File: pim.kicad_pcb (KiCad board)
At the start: 2 copper layers, 96.4 x 66.5 mm, 13 parts, among them J1 DE9_Plug, J2 DE9_Plug, J3 Conn_01x20_Pin, J4 Conn_01x03_MountingPin, U1 RaspberryPi_Pico_W

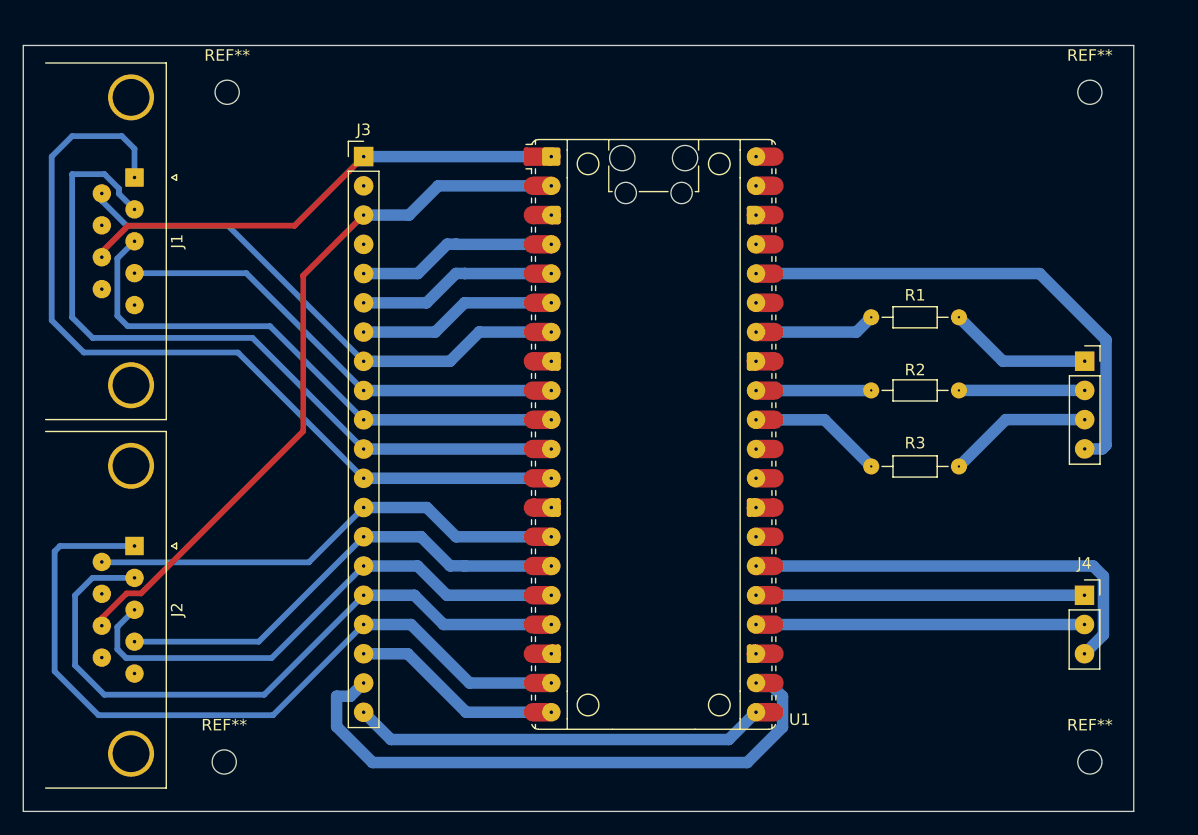
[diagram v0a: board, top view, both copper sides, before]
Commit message: improve some tracks cleareance
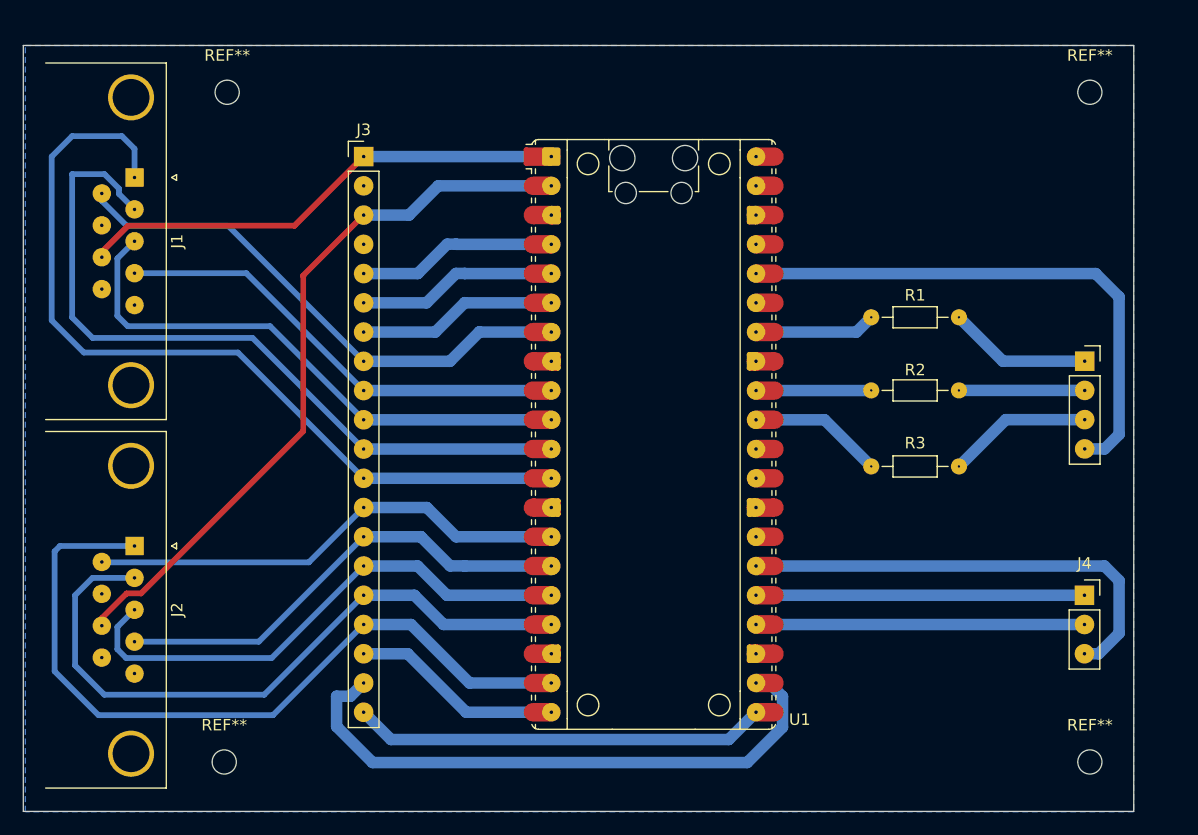
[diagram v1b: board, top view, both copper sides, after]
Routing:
- net Net-(D1-A): track 43.9 -> 47.8 mm
- net /PI-11: track 38.0 -> 40.4 mm
- added copper zone on B.Cu, net GNDPWR
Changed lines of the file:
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@@
 		(fp_arc
 			(start 10.579676 25.189937)
-			(mid 10.357946 25.493957)
+			(mid 10.35796 25.493961)
 			(end 10 25.61)
 			(stroke
@@
 	)
 	(segment
-		(start 108.166428 33.782)
-		(end 113.923428 39.539)
+		(start 115.062 35.814)
+		(end 115.062 47.752)
 		(width 1)
 		(layer "B.Cu")
@@
 	)
 	(segment
-		(start 113.597428 49.009)
+		(start 113.805 49.009)
 		(end 112.073428 49.009)
 		(width 1)
@@
 	)
 	(segment
-		(start 113.923428 39.539)
-		(end 113.923428 48.683)
+		(start 83.527428 33.782)
+		(end 113.03 33.782)
 		(width 1)
 		(layer "B.Cu")
@@
 	)
 	(segment
-		(start 113.923428 48.683)
-		(end 113.597428 49.009)
+		(start 113.03 33.782)
+		(end 115.062 35.814)
 		(width 1)
 		(layer "B.Cu")
@@
 	)
 	(segment
-		(start 83.527428 33.782)
-		(end 108.166428 33.782)
+		(start 115.062 47.752)
+		(end 113.805 49.009)
 		(width 1)
 		(layer "B.Cu")
@@
 	)
 	(segment
-		(start 28.196331 26.858)
-		(end 29.546331 28.208)
-		(width 0.5)
-		(layer "B.Cu")
-		(net 16)
-	)
-	(segment
-		(start 28.196331 26.403811)
-		(end 28.196331 26.858)
+		(start 24.13 37.592)
+		(end 24.13 25.146)
 		(width 0.5)
 		(layer "B.Cu")
@@
 	)
 	(segment
-		(start 24.13 37.592)
-		(end 24.13 25.146)
+		(start 28.196331 26.858)
+		(end 29.546331 28.208)
 		(width 0.5)
 		(layer "B.Cu")
@@
 	)
 	(segment
-		(start 25.908 39.37)
-		(end 24.13 37.592)
+		(start 24.13 25.146)
+		(end 26.93852 25.146)
 		(width 0.5)
 		(layer "B.Cu")
@@
 	)
 	(segment
-		(start 24.13 25.146)
-		(end 26.93852 25.146)
+		(start 26.93852 25.146)
+		(end 28.196331 26.403811)
 		(width 0.5)
 		(layer "B.Cu")
@@
 	)
 	(segment
-		(start 49.447428 49.022)
-		(end 39.795428 39.37)
+		(start 25.908 39.37)
+		(end 24.13 37.592)
 		(width 0.5)
 		(layer "B.Cu")
@@
 	)
 	(segment
-		(start 26.93852 25.146)
-		(end 28.196331 26.403811)
+		(start 28.196331 26.403811)
+		(end 28.196331 26.858)
 		(width 0.5)
 		(layer "B.Cu")
@@
 	)
 	(segment
+		(start 49.447428 49.022)
+		(end 39.795428 39.37)
+		(width 0.5)
+		(layer "B.Cu")
+		(net 16)
+	)
+	(segment
 		(start 56.955428 59.169)
 		(end 58.225428 59.169)
@@
 	)
 	(segment
-		(start 83.527428 59.182)
-		(end 112.812 59.182)
+		(start 115.062 60.452)
+		(end 115.062 65.024)
 		(width 1)
 		(layer "B.Cu")
@@
 	)
 	(segment
-		(start 113.702 60.072)
-		(end 113.702 65.152)
+		(start 113.792 59.182)
+		(end 115.062 60.452)
 		(width 1)
 		(layer "B.Cu")
@@
 	)
 	(segment
-		(start 112.812 59.182)
-		(end 113.702 60.072)
+		(start 83.527428 59.182)
+		(end 113.792 59.182)
 		(width 1)
 		(layer "B.Cu")
@@
 	)
 	(segment
-		(start 113.702 65.152)
+		(start 115.062 65.024)
+		(end 113.284 66.802)
+		(width 1)
+		(layer "B.Cu")
+		(net 44)
+	)
+	(segment
+		(start 113.284 66.802)
 		(end 112.052 66.802)
 		(width 1)
@@
 		(net 45)
 	)
+	(zone
+		(net 42)
+		(net_name "GNDPWR")
+		(layer "B.Cu")
+		(name "GND")
+		(hatch edge 0.5)
+		(connect_pads
+			(clearance 0.5)
+		)
+		(min_thickness 0.5)
+		(filled_areas_thickness no)
+		(fill
+			(thermal_gap 0.5)
+			(thermal_bridge_width 0.5)
+		)
+		(polygon
+			(pts
+				(xy 116.332 13.97) (xy 116.332 80.518) (xy 20.066 80.518) (xy 20.066 13.97)
+			)
+		)
+	)
 )

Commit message: pimmo-control-64 label
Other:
- board text added: "PIMMO-PORTS-64"
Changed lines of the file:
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@@
 		(layer "Edge.Cuts")
+	)
+	(gr_text "PIMMO-PORTS-64"
+		(at 87.376 77.47 0)
+		(layer "B.Cu")
+		(effects
+			(font
+				(size 1.5 1.5)
+				(thickness 0.3)
+				(bold yes)
+			)
+			(justify right bottom mirror)
+		)
 	)
 	(segment

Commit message: Some minor improvements
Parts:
- moved REF** 3.56 mm to (116.1, 76.2)
- moved REF** 3.53 mm to (115.6, 16.3)
- moved REF** 1.55 mm to (37.3, 16.5)
- moved REF** 0.25 mm to (37.1, 76.2)
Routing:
- net /M-8: track 63.2 -> 75.1 mm, vias 0 -> 2
- net /M-i: track 42.9 -> 52.6 mm, vias 0 -> 2
- net /M-e: track 58.9 -> 60.9 mm
- removed copper zone on B.Cu, net GNDPWR
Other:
- board size 96.4 x 66.5 mm -> 100 x 65.3 mm
